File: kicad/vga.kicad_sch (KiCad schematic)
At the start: 30 parts, among them J3 DE15_Receptacle_HighDensity_M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, Q1 BC547, U10 6264, U12 74HC574, U13 74HC174, U14 2764, U15 74HC166, U4 74HC244, U5 XC9536PC44, U6 74HC244, U7 74HC02, U9 74HC245

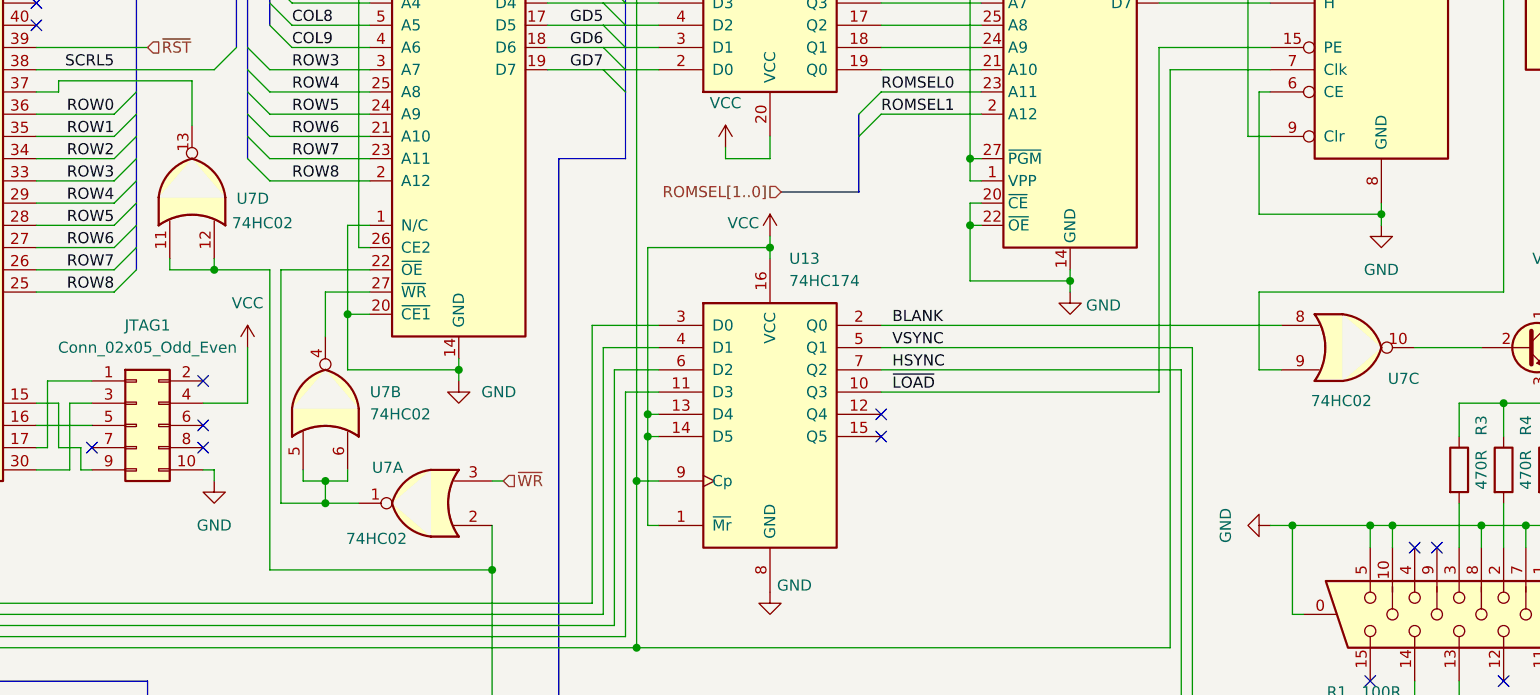
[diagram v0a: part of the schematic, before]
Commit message: hw: simplify logic, replace some SSI with GALs
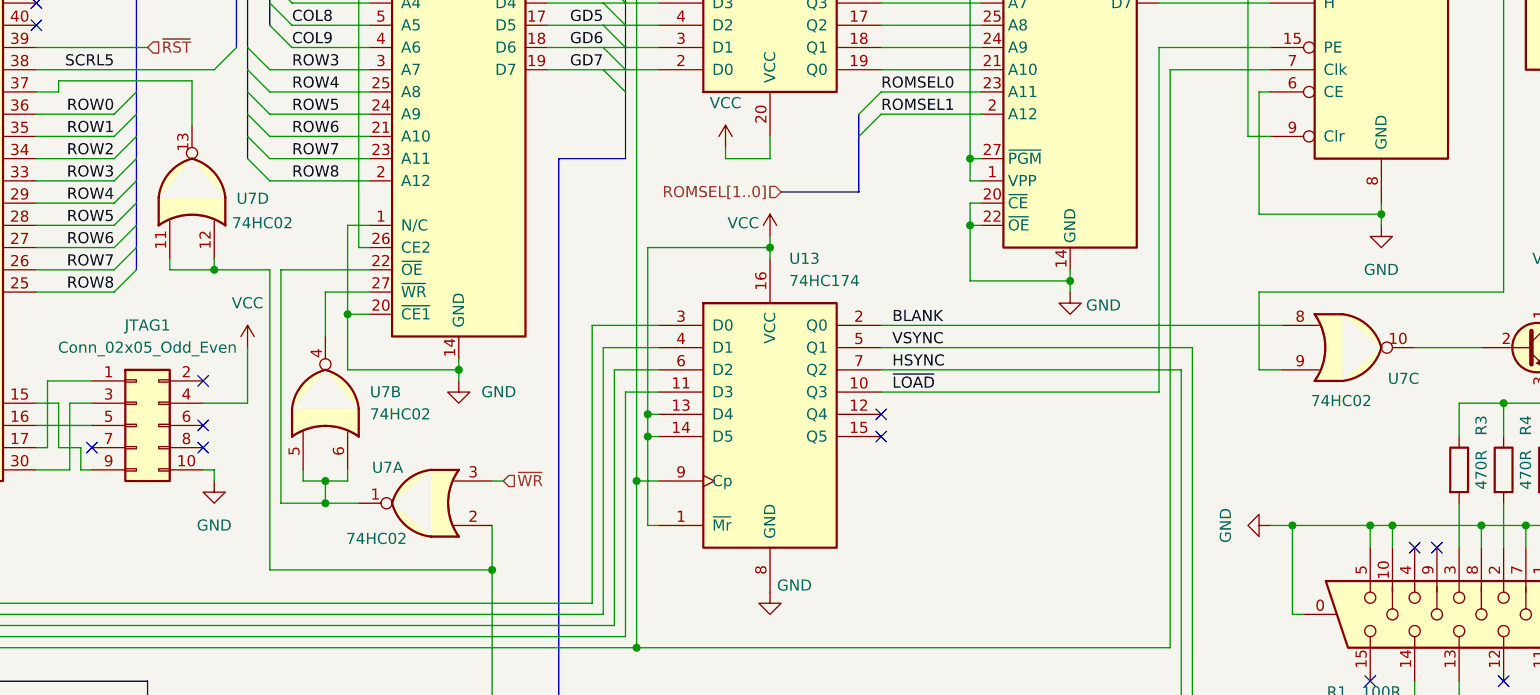
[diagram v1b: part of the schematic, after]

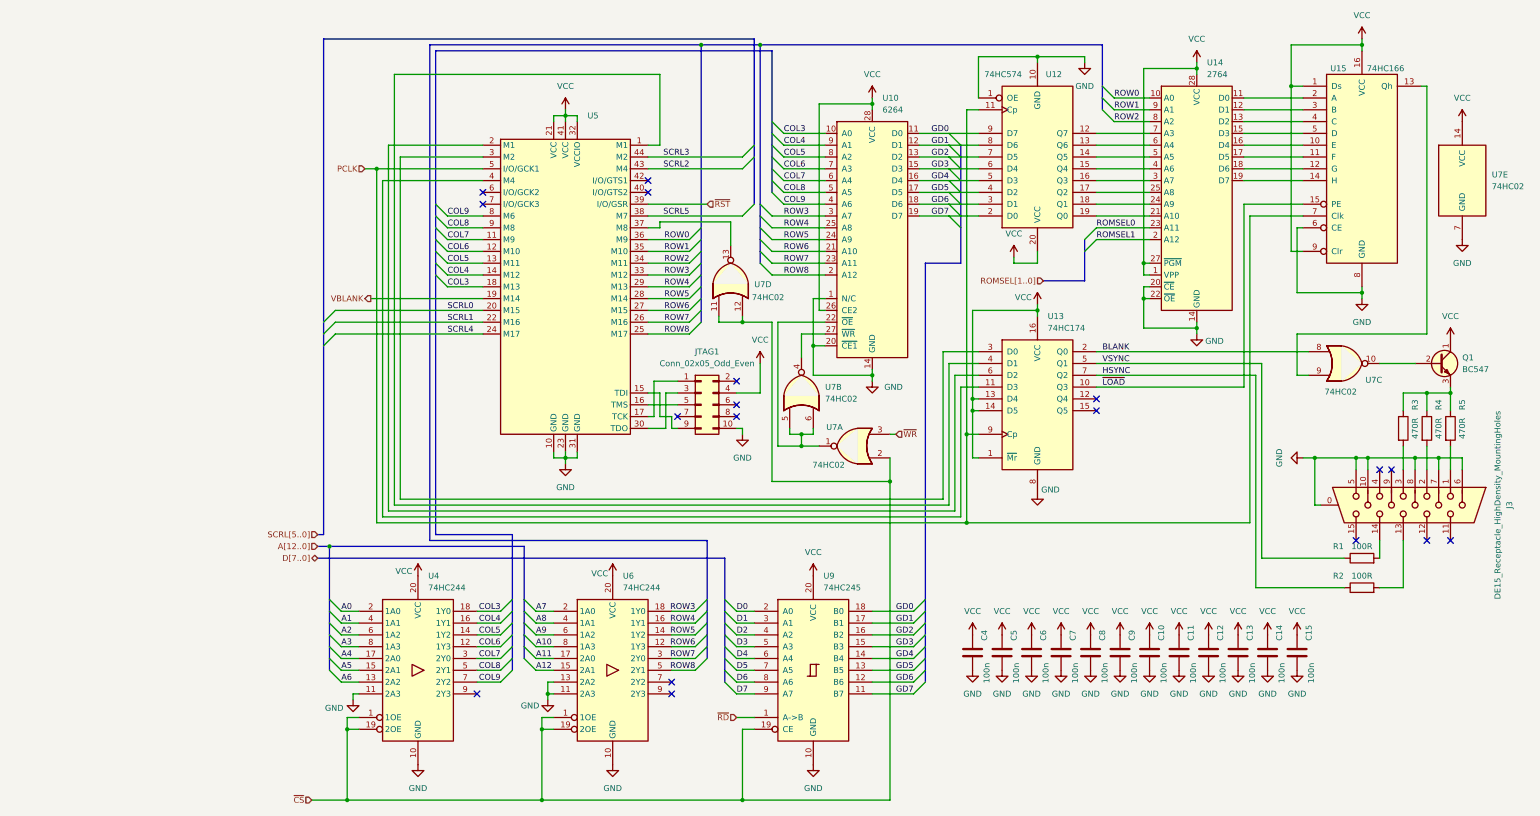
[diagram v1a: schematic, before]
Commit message: hw: color text mode VGA (WIP)
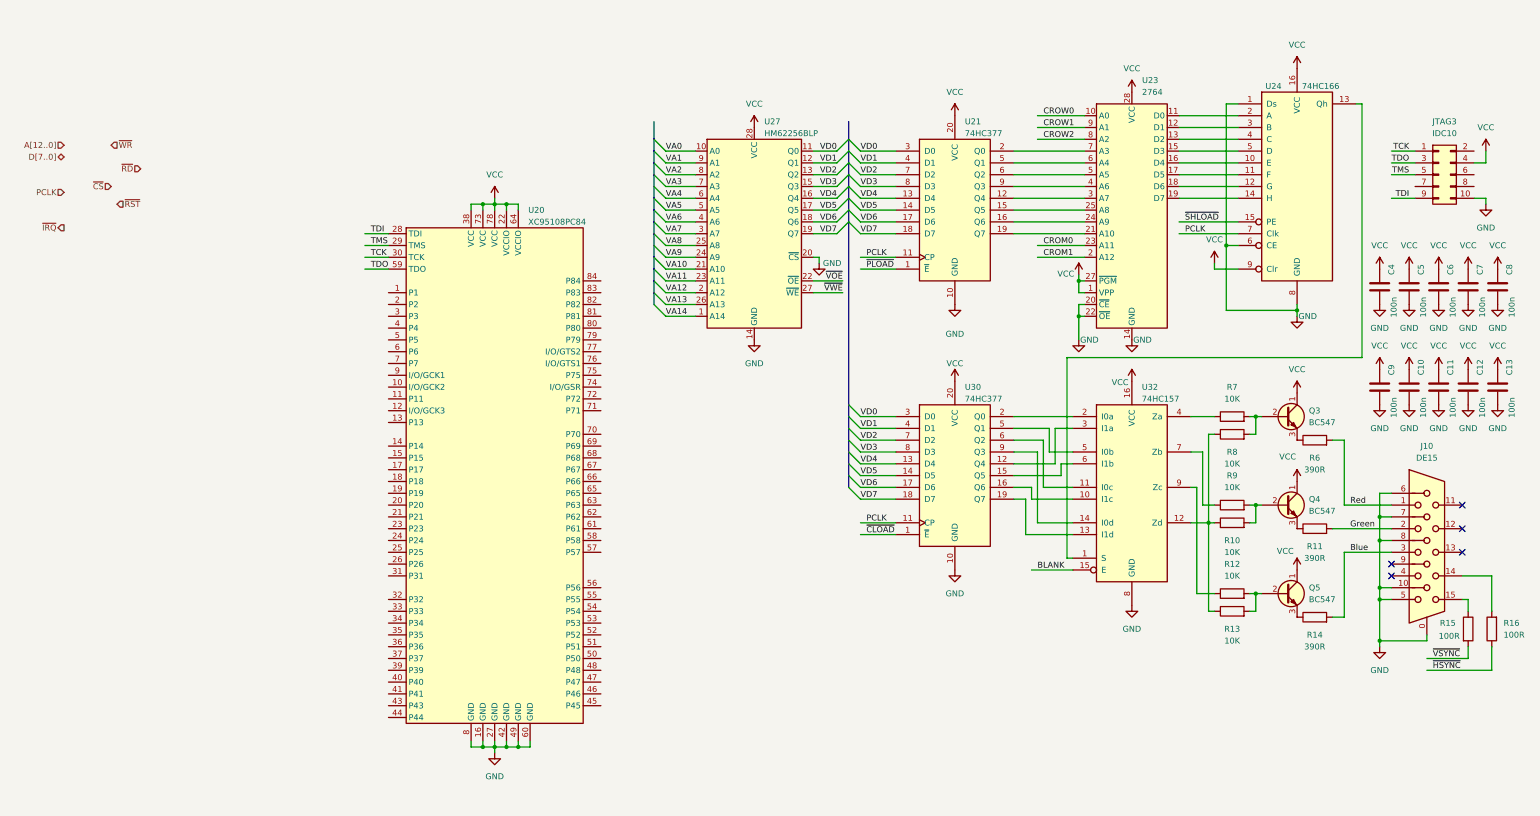
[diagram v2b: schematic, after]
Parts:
- removed C14, C15: 100n, Capacitor_THT:C_Disc_D5.0mm_W2.5mm_P2.50mm, symbol Device:C
- removed J3: DE15_Receptacle_HighDensity_MountingHoles, Connector_Dsub:DSUB-15-HD_Female_Horizontal_P2.29x1.98mm_EdgePinOffset3.03mm_Housed_MountingHolesOffset4.94mm, symbol Connector:DE15_Receptacle_HighDensity_MountingHoles
- removed JTAG1: Conn_02x05_Odd_Even, Connector_IDC:IDC-Header_2x05_P2.54mm_Vertical, symbol Connector_Generic:Conn_02x05_Odd_Even
- removed Q1: BC547, Package_TO_SOT_THT:TO-92, symbol PCM_Transistor_BJT_AKL:BC547
- removed R1, R2: 100R, Resistor_THT:R_Axial_DIN0207_L6.3mm_D2.5mm_P7.62mm_Horizontal, symbol Device:R
- removed R3, R4, R5: 470R, Resistor_THT:R_Axial_DIN0207_L6.3mm_D2.5mm_P7.62mm_Horizontal, symbol Device:R
- removed U10: 6264, PCM_Package_DIP_AKL:DIP-28_W15.24mm, symbol 8bits:6264
- removed U12: 74HC574, PCM_Package_DIP_AKL:DIP-20_W7.62mm, symbol 74xx:74HCT574
- removed U13: 74HC174, Package_DIP:DIP-16_W7.62mm, symbol 74xx:74LS174
- removed U14: 2764, Package_DIP:DIP-28_W15.24mm, symbol Memory_EPROM:2764
- removed U15: 74HC166, Package_DIP:DIP-16_W7.62mm, symbol 74xx:74LS166
- removed U4, U6: 74HC244, Package_DIP:DIP-20_W7.62mm, symbol 74xx:74HC244
- removed U5: XC9536PC44, Package_LCC:PLCC-44_THT-Socket, symbol CPLD_Xilinx:XC9536PC44
- removed U7: 74HC02, PCM_Package_DIP_AKL:DIP-14_W7.62mm, symbol 74xx:74HC02
- removed U9: 74HC245, Package_DIP:DIP-20_W7.62mm, symbol 74xx:74HC245
- added J10: DE15, Connector_Dsub:DSUB-15-HD_Female_Horizontal_P2.29x1.98mm_EdgePinOffset3.03mm_Housed_MountingHolesOffset4.94mm, symbol Connector:DE15_Receptacle_HighDensity_MountingHoles
- added JTAG3: IDC10, Connector_IDC:IDC-Header_2x05_P2.54mm_Vertical, symbol Connector_Generic:Conn_02x05_Odd_Even
- added Q3, Q4, Q5: BC547, Package_TO_SOT_THT:TO-92, symbol PCM_Transistor_BJT_AKL:BC547
- added R10, R12, R13, R7, R8, R9: 10K, Resistor_THT:R_Axial_DIN0207_L6.3mm_D2.5mm_P7.62mm_Horizontal, symbol Device:R
- added R11, R14, R6: 390R, Resistor_THT:R_Axial_DIN0207_L6.3mm_D2.5mm_P7.62mm_Horizontal, symbol Device:R
- added R15, R16: 100R, Resistor_THT:R_Axial_DIN0207_L6.3mm_D2.5mm_P7.62mm_Horizontal, symbol Device:R
- added U20: XC95108PC84, Package_LCC:PLCC-84, symbol CPLD_Xilinx:XC95108PC84
- added U21, U30: 74HC377, Package_DIP:DIP-20_W7.62mm, symbol 74xx:74LS377
- added U23: 2764, Package_DIP:DIP-28_W15.24mm, symbol Memory_EPROM:2764
- added U24: 74HC166, Package_DIP:DIP-16_W7.62mm, symbol 74xx:74LS166
- added U27: HM62256BLP, Package_DIP:DIP-28_W15.24mm, symbol Memory_RAM:HM62256BLP
- added U32: 74HC157, Package_DIP:DIP-16_W7.62mm, symbol 74xx:74LS157
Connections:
- net BLANK: now also U32.15 (E)
- net GND: now also J10.0, J10.10, J10.5, J10.6, J10.7, J10.8, JTAG3.10 (Pin_10), U20.16 (GND), U20.27 (GND), U20.42 (GND), U20.49 (GND), U20.60 (GND), U20.8 (GND), U21.10 (GND), U23.14 (GND), U23.20 (~{CE}), U23.22 (~{OE}), U24.1 (Ds), U24.6 (CE), U24.8 (GND), U27.14 (GND), U27.20 (~{CS}), U30.10 (GND), U32.8 (GND)
- net PCLK: now also U21.11 (CP), U24.7 (Clk), U30.11 (CP)
- net VCC: now also JTAG3.4 (Pin_4), Q3.1 (C), Q4.1 (C), Q5.1 (C), U20.22 (VCCIO), U20.38 (VCC), U20.64 (VCCIO), U20.73 (VCC), U20.78 (VCC), U21.20 (VCC), U23.1 (VPP), U23.27 (~{PGM}), U23.28 (VCC), U24.16 (VCC), U24.9 (Clr), U27.28 (VCC), U30.20 (VCC), U32.16 (VCC)
- new net: U21.12 (Q4), U23.3 (A7)
- new net: U21.15 (Q5), U23.25 (A8)
- new net: U21.16 (Q6), U23.24 (A9)
- new net: U21.19 (Q7), U23.21 (A10)
- new net: U21.2 (Q0), U23.7 (A3)
- new net: U21.5 (Q1), U23.6 (A4)
- new net: U21.6 (Q2), U23.5 (A5)
- new net: U21.9 (Q3), U23.4 (A6)
- new net: U24.13 (Qh), U32.1 (S)
- new net: U30.16 (Q6), U32.10 (I1c)
- new net: U30.6 (Q2), U32.11 (I0c)
- new net: R10.1, R13.1, R8.1, U32.12 (Zd)
- new net: U30.19 (Q7), U32.13 (I1d)
- new net: U30.9 (Q3), U32.14 (I0d)
- new net: U30.2 (Q0), U32.2 (I0a)
- new net: U30.12 (Q4), U32.3 (I1a)
- new net: R7.1, U32.4 (Za)
- new net: U30.5 (Q1), U32.5 (I0b)
- new net: U30.15 (Q5), U32.6 (I1b)
- new net: R9.1, U32.7 (Zb)
- new net: R12.1, U32.9 (Zc)
- new net: Q3.2 (B), R7.2, R8.2
- new net: Q3.3 (E), R6.1
- new net: Q4.2 (B), R10.2, R9.2
- new net: J10.14, R16.2
- new net: J10.15, R15.1
- new net: Q5.2 (B), R12.2, R13.2
- new net: U23.11 (D0), U24.2 (A)
- new net: U23.12 (D1), U24.3 (B)
- new net: U23.13 (D2), U24.4 (C)
- new net: U23.15 (D3), U24.5 (D)
- new net: U23.16 (D4), U24.10 (E)
- new net: U23.17 (D5), U24.11 (F)
- new net: U23.18 (D6), U24.12 (G)
- new net: U23.19 (D7), U24.14 (H)
- new net: Q4.3 (E), R11.1
- new net: Q5.3 (E), R14.1
- new net Blue: J10.3, R14.2
- new net CROM0: U23.23 (A11)
- new net CROM1: U23.2 (A12)
- new net CROW0: U23.10 (A0)
- new net CROW1: U23.9 (A1)
- new net CROW2: U23.8 (A2)
- new net Green: J10.2, R11.2
- new net Red: J10.1, R6.2
- new net TCK: JTAG3.1 (Pin_1), U20.30 (TCK)
- new net TDI: JTAG3.9 (Pin_9), U20.28 (TDI)
- new net TDO: JTAG3.3 (Pin_3), U20.59 (TDO)
- new net TMS: JTAG3.5 (Pin_5), U20.29 (TMS)
- new net VA0: U27.10 (A0)
- new net VA1: U27.9 (A1)
- new net VA10: U27.21 (A10)
- new net VA11: U27.23 (A11)
- new net VA12: U27.2 (A12)
- new net VA13: U27.26 (A13)
- new net VA14: U27.1 (A14)
- new net VA2: U27.8 (A2)
- new net VA3: U27.7 (A3)
- new net VA4: U27.6 (A4)
- new net VA5: U27.5 (A5)
- new net VA6: U27.4 (A6)
- new net VA7: U27.3 (A7)
- new net VA8: U27.25 (A8)
- new net VA9: U27.24 (A9)
- new net VD0: U21.3 (D0), U27.11 (Q0), U30.3 (D0)
- new net VD1: U21.4 (D1), U27.12 (Q1), U30.4 (D1)
- new net VD2: U21.7 (D2), U27.13 (Q2), U30.7 (D2)
- new net VD3: U21.8 (D3), U27.15 (Q3), U30.8 (D3)
- new net VD4: U21.13 (D4), U27.16 (Q4), U30.13 (D4)
- new net VD5: U21.14 (D5), U27.17 (Q5), U30.14 (D5)
- new net VD6: U21.17 (D6), U27.18 (Q6), U30.17 (D6)
- new net VD7: U21.18 (D7), U27.19 (Q7), U30.18 (D7)
- new net ~{CLOAD}: U30.1 (~{E})
- new net ~{HSYNC}: R16.1
- new net ~{PLOAD}: U21.1 (~{E})
- new net ~{SHLOAD}: U24.15 (PE)
- new net ~{VOE}: U27.22 (~{OE})
- new net ~{VSYNC}: R15.2
- new net ~{VWE}: U27.27 (~{WE})
- no-connect marks 18 -> 5
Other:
- moved on the sheet: C10, C11, C12, C13, C4, C5, C6, C7, C8, C9

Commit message: hw: finish schematic, start routing
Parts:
- removed C10, C11, C12, C13, C4, C5, C6, C7, C8, C9: 100n, Capacitor_THT:C_Disc_D5.0mm_W2.5mm_P2.50mm, symbol Device:C
- removed Q3, Q4, Q5: BC547, Package_TO_SOT_THT:TO-92, symbol PCM_Transistor_BJT_AKL:BC547
- removed R10, R12, R13, R7, R8, R9: 10K, Resistor_THT:R_Axial_DIN0207_L6.3mm_D2.5mm_P7.62mm_Horizontal, symbol Device:R
- removed R11, R14, R6: 390R, Resistor_THT:R_Axial_DIN0207_L6.3mm_D2.5mm_P7.62mm_Horizontal, symbol Device:R
- removed U21, U30: 74HC377, Package_DIP:DIP-20_W7.62mm, symbol 74xx:74LS377
- removed U23: 2764, Package_DIP:DIP-28_W15.24mm, symbol Memory_EPROM:2764
- removed U24: 74HC166, Package_DIP:DIP-16_W7.62mm, symbol 74xx:74LS166
- removed U27: HM62256BLP, Package_DIP:DIP-28_W15.24mm, symbol Memory_RAM:HM62256BLP
- removed U32: 74HC157, Package_DIP:DIP-16_W7.62mm, symbol 74xx:74LS157
- J10: footprint Connector_Dsub:DSUB-15-HD_Female_Horizontal_P2.29x1.98mm_EdgePinOffset3.03mm_Housed_MountingHolesOffset4.94mm -> Connector_Dsub:DSUB-15-HD_Socket_Horizontal_P2.29x1.90mm_EdgePinOffset3.03mm_Housed_MountingHolesOffset4.94mm
- U20: footprint Package_LCC:PLCC-84 -> Package_LCC:PLCC-84_THT-Socket
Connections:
- net BLANK: now also U20.76 (I/O/GTS1)
- net CROW0: now also U20.56 (P56)
- net CROW1: now also U20.55 (P55)
- net CROW2: now also U20.54 (P54)
- net PCLK: now also U20.9 (I/O/GCK1)
- net VA0: now also U20.31 (P31)
- net VA1: now also U20.26 (P26)
- net VA10: now also U20.6 (P6)
- net VA11: now also U20.11 (P11)
- net VA12: now also U20.18 (P18)
- net VA13: now also U20.15 (P15)
- net VA2: now also U20.25 (P25)
- net VA3: now also U20.24 (P24)
- net VA4: now also U20.23 (P23)
- net VA5: now also U20.21 (P21)
- net VA6: now also U20.20 (P20)
- net VA7: now also U20.19 (P19)
- net VA8: now also U20.14 (P14)
- net VA9: now also U20.13 (P13)
- net VD0: now also U20.32 (P32)
- net VD1: now also U20.34 (P34)
- net VD2: now also U20.33 (P33)
- net VD3: now also U20.1 (P1)
- net VD4: now also U20.2 (P2)
- net VD5: now also U20.3 (P3)
- net VD6: now also U20.4 (P4)
- net VD7: now also U20.5 (P5)
- net ~{CLOAD}: now also U20.84 (P84)
- net ~{CS}: now also U20.80 (P80)
- net ~{HSYNC}: now also U20.81 (P81)
- net ~{IRQ}: now also U20.44 (P44)
- net ~{PLOAD}: now also U20.83 (P83)
- net ~{RD}: now also U20.77 (I/O/GTS2)
- net ~{RST}: now also U20.74 (I/O/GSR)
- net ~{VOE}: now also U20.7 (P7)
- net ~{VSYNC}: now also U20.82 (P82)
- net ~{VWE}: now also U20.17 (P17)
- net ~{WR}: now also U20.79 (P79)
- net SCROLL0: now reaches U20.35 (P35)
- net SCROLL1: now reaches U20.36 (P36)
- net SCROLL2: now reaches U20.37 (P37)
- net SCROLL3: now reaches U20.39 (P39)
- net SCROLL4: now reaches U20.40 (P40)
- net SCROLL5: now reaches U20.41 (P41)
- net ~{IRQACK}: now reaches U20.43 (P43)
- net D3: now reaches U20.45 (P45)
- net D2: now reaches U20.46 (P46)
- net D4: now reaches U20.47 (P47)
- net D1: now reaches U20.48 (P48)
- net D5: now reaches U20.50 (P50)
- net D0: now reaches U20.51 (P51)
- net D6: now reaches U20.52 (P52)
- net D7: now reaches U20.53 (P53)
- net A12: now reaches U20.57 (P57)
- net A11: now reaches U20.58 (P58)
- net A13: now reaches U20.61 (P61)
- net A9: now reaches U20.62 (P62)
- net A10: now reaches U20.63 (P63)
- net A7: now reaches U20.65 (P65)
- net A8: now reaches U20.66 (P66)
- net A5: now reaches U20.67 (P67)
- net A6: now reaches U20.68 (P68)
- net A4: now reaches U20.69 (P69)
- net A2: now reaches U20.70 (P70)
- net A3: now reaches U20.71 (P71)
- net A0: now reaches U20.72 (P72)
- net A1: now reaches U20.75 (P75)
- net Blue renamed vga_datapath/BLUE
- net Green renamed vga_datapath/GREEN
- net Red renamed vga_datapath/RED
- no-connect marks 5 -> 11
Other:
- added sheet vga_datapath (vga_datapath.kicad_sch)
- company: (none) -> A.K.
- title: (none) -> VGA
- moved on the sheet: J10, JTAG3, R15, R16, U20
